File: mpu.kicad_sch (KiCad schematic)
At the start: 0 parts

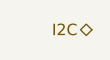
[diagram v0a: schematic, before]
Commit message: Fixed bus names
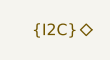
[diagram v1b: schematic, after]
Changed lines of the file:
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@@
     (title "Phoenix MPU")
   )
-  (hierarchical_label "I2C" (shape bidirectional) (at 21.59 20.32 180)
+  (hierarchical_label "{I2C}" (shape bidirectional) (at 21.59 20.32 180)
     (effects (font (size 1.27 1.27)) (justify right))
   )
